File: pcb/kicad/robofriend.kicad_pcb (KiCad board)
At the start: 2 copper layers, 122 parts, among them J1 UART, J10 12V-Buck, J11 12V-Buck-Boost, J12 5VIN, J13 5VOUT, J14 5VOUT, J15 US2, J16 US3, J17 USB_A_4_PIN, J18 12V-Reg, J19 MON/AMP, J2 PWR, J20 US4, J21 MRi, J22 SPI, J23 MLe, J24 3V3OUT, J25 3V3OUT, J26 M1, J27 M2, J28 IR1, J29 ADC1, J3 PWR, J30 IR2, J31 ADC2, J32 IR3, J33 GS2, J4 GS2, J5 I2C, J6 I2C, J7 I2C, J8 I2C, J9 US1, K1 SCHRACK-RTx3, Q1 NMOS, Q2 NPN, Q3 PMOS, U1 74LVC1T45, U10 TL331, U2 Teensy++2.0, U3 TL331, U4 74LVC1T45, U5 PCA9517, U6 MCP6001, U7 LM3940-3.3, U8 LM4040, U9 INA193

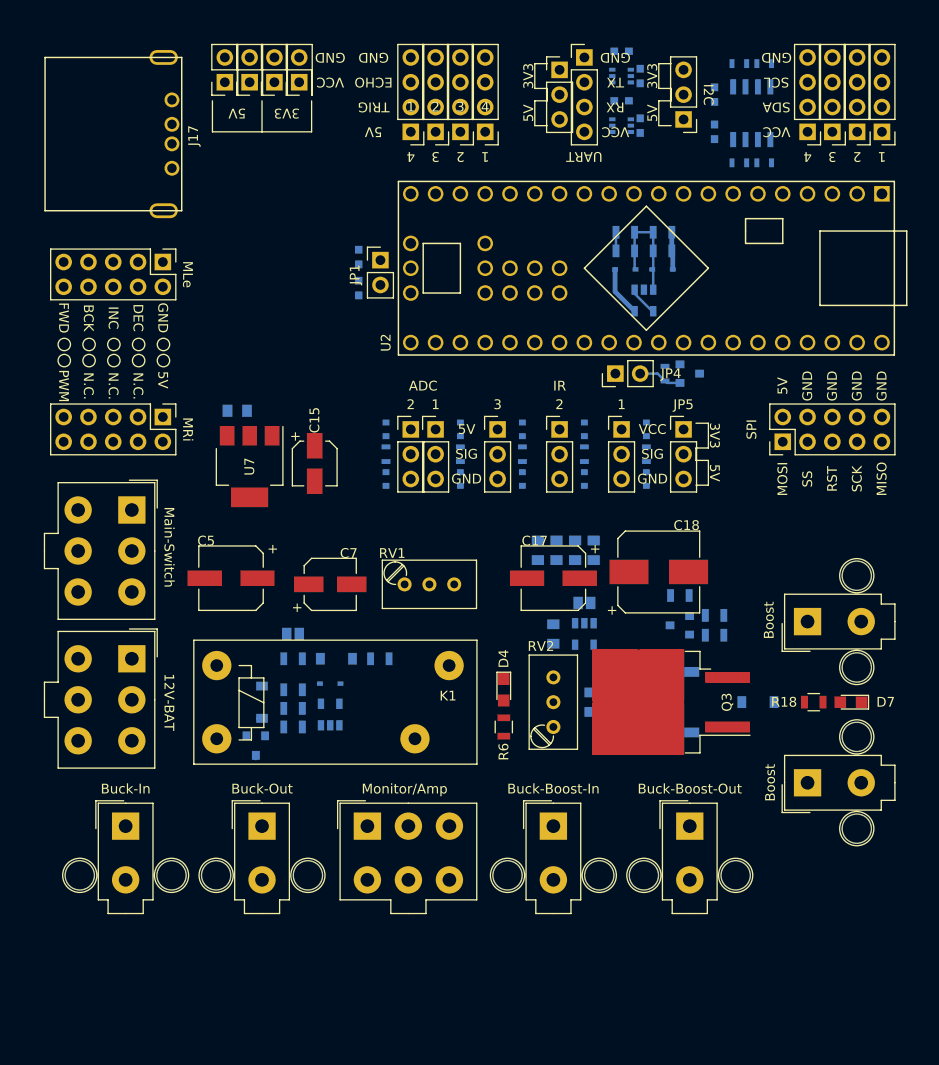
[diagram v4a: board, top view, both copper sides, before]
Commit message: defined board edge cuts
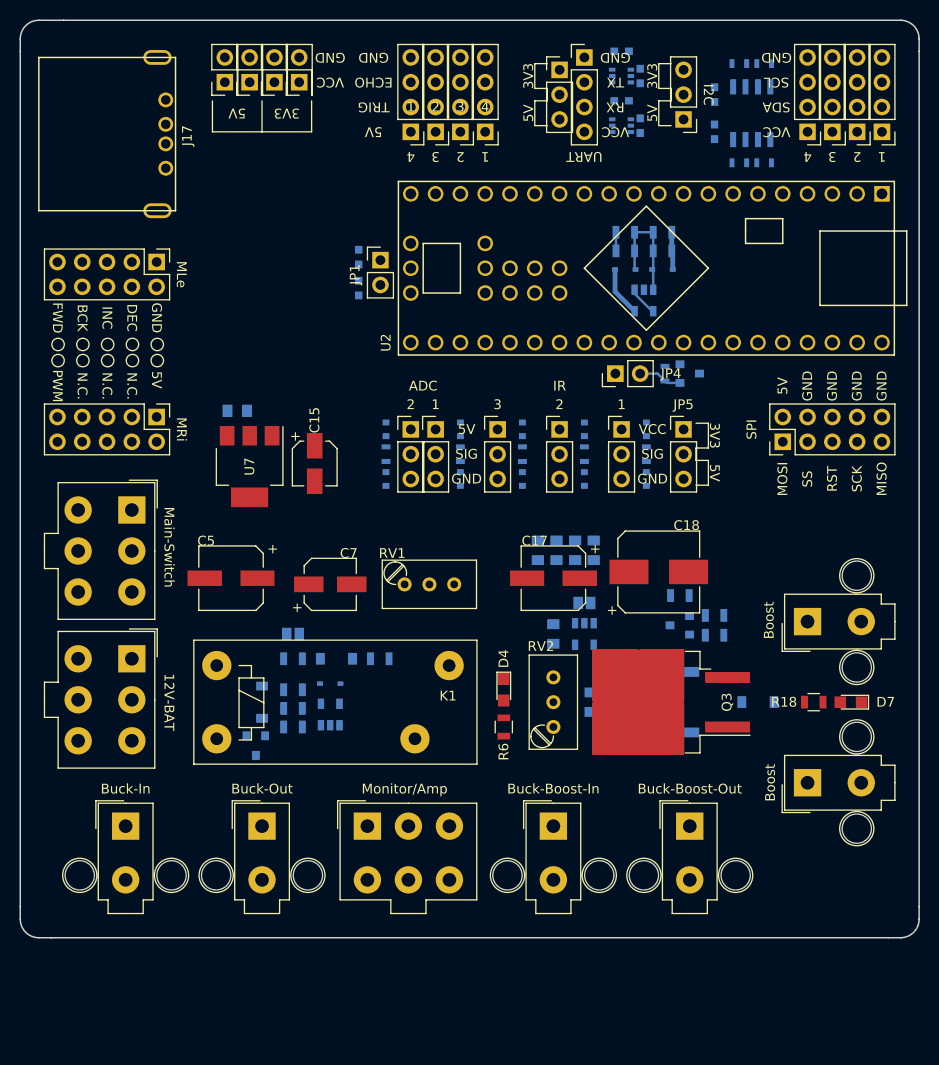
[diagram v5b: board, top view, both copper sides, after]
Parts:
- moved J17 0.64 mm to (82.5, 71.1)
- moved J21 0.64 mm to (94.6, 108.0)
- moved J23 0.64 mm to (94.6, 92.1)
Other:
- board outline added: 92.1 x 94 mm
- net class 10A: clearance 0.2 -> 0.254
- net class 3A: clearance 0.2 -> 0.254
- net class 5A: clearance 0.2 -> 0.254
- net class Default: clearance 0.2 -> 0.254; trace_width 0.25 -> 0.254
- rule trace_clearance: 0.2 -> 0.254
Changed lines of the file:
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@@
     (links 300)
     (no_connects 285)
-    (area 80.93 67.38 172.315 159.385001)
+    (area 80.295 67.234999 172.795001 161.365001)
     (thickness 1.6)
-    (drawings 119)
+    (drawings 134)
     (tracks 28)
     (zones 0)
@@
   )
   (setup
-    (last_trace_width 0.25)
-    (trace_clearance 0.2)
+    (last_trace_width 0.254)
+    (trace_clearance 0.254)
     (zone_clearance 0.508)
     (zone_45_only no)
     (trace_min 0.2)
-    (segment_width 0.1)
+    (segment_width 0.35)
     (edge_width 0.15)
     (via_size 0.6)
@@
   (net 77 "Net-(JP4-Pad2)")
   (net_class Default "This is the default net class."
-    (clearance 0.2)
-    (trace_width 0.25)
+    (clearance 0.254)
+    (trace_width 0.254)
     (via_dia 0.6)
     (via_drill 0.4)
@@
   )
   (net_class 10A ""
-    (clearance 0.2)
+    (clearance 0.254)
     (trace_width 2)
     (via_dia 0.6)
@@
   )
   (net_class 3A ""
-    (clearance 0.2)
+    (clearance 0.254)
     (trace_width 0.48)
     (via_dia 0.6)
@@
   )
   (net_class 5A ""
-    (clearance 0.2)
+    (clearance 0.254)
     (trace_width 0.96)
     (via_dia 0.6)
@@
     (tags "capacitor 0805")
     (attr smd)
-    (fp_text reference C11 (at -0.3175 -1.5875) (layer B.SilkS)
+    (fp_text reference C11 (at 0 -1.905) (layer B.SilkS)
       (effects (font (size 1 1) (thickness 0.15)) (justify mirror))
     )
@@
   )
   (module Pin_Headers:Pin_Header_Straight_2x05_Pitch2.54mm (layer F.Cu)
-    (at 95.25 107.95 270)
+    (at 94.615 107.95 270)
     (descr "Through hole straight pin header, 2x05, 2.54mm pitch, double rows")
     (tags "Through hole pin header THT 2x05 2.54mm double row")
@@
   )
   (module Pin_Headers:Pin_Header_Straight_2x05_Pitch2.54mm (layer F.Cu)
-    (at 95.25 92.075 270)
+    (at 94.615 92.075 270)
     (descr "Through hole straight pin header, 2x05, 2.54mm pitch, double rows")
     (tags "Through hole pin header THT 2x05 2.54mm double row")
@@
   )
   (module USB_A_4_PIN:MOLEX_48258_0001 (layer F.Cu)
-    (at 83.185 71.12 270)
+    (at 82.55 71.12 270)
     (descr "USB A connector")
     (tags "USB USB_A")
@@
     )
   )
+  (gr_arc (start 82.55 159.385) (end 82.55 161.29) (angle 90) (layer Edge.Cuts) (width 0.15))
+  (gr_arc (start 170.815 159.385) (end 172.72 159.385) (angle 90) (layer Edge.Cuts) (width 0.15))
+  (gr_arc (start 170.815 69.215) (end 170.815 67.31) (angle 90) (layer Edge.Cuts) (width 0.15))
+  (gr_arc (start 82.55 69.215) (end 80.645 69.215) (angle 90) (layer Edge.Cuts) (width 0.15))
+  (gr_line (start 85.09 67.31) (end 82.55 67.31) (angle 90) (layer Edge.Cuts) (width 0.15))
+  (gr_line (start 80.645 70.485) (end 80.645 69.215) (angle 90) (layer Edge.Cuts) (width 0.15))
+  (gr_line (start 83.82 161.29) (end 82.55 161.29) (angle 90) (layer Edge.Cuts) (width 0.15))
+  (gr_line (start 80.645 158.115) (end 80.645 159.385) (angle 90) (layer Edge.Cuts) (width 0.15))
+  (gr_line (start 170.815 161.29) (end 169.545 161.29) (angle 90) (layer Edge.Cuts) (width 0.15))
+  (gr_line (start 172.72 159.385) (end 172.72 158.115) (angle 90) (layer Edge.Cuts) (width 0.15))
+  (gr_line (start 172.72 70.485) (end 172.72 69.215) (angle 90) (layer Edge.Cuts) (width 0.15))
+  (gr_line (start 80.645 158.115) (end 80.645 70.485) (angle 90) (layer Edge.Cuts) (width 0.15))
+  (gr_line (start 169.545 161.29) (end 83.82 161.29) (angle 90) (layer Edge.Cuts) (width 0.15))
+  (gr_line (start 172.72 70.485) (end 172.72 158.115) (angle 90) (layer Edge.Cuts) (width 0.15))
+  (gr_line (start 85.09 67.31) (end 170.815 67.31) (angle 90) (layer Edge.Cuts) (width 0.15))
   (gr_line (start 133.35 71.755) (end 133.35 74.295) (angle 90) (layer F.SilkS) (width 0.1))
   (gr_line (start 134.62 74.295) (end 134.62 75.565) (angle 90) (layer F.SilkS) (width 0.1))
@@
     (effects (font (size 1 1) (thickness 0.15)))
   )
-  (gr_circle (center 85.1535 100.5205) (end 85.1535 101.1555) (layer F.SilkS) (width 0.1))
-  (gr_circle (center 85.1535 102.1715) (end 85.1535 102.8065) (layer F.SilkS) (width 0.1))
-  (gr_circle (center 90.2335 100.5205) (end 90.2335 101.1555) (layer F.SilkS) (width 0.1))
-  (gr_circle (center 90.2335 102.1715) (end 90.2335 102.8065) (layer F.SilkS) (width 0.1))
-  (gr_circle (center 87.6935 102.1715) (end 87.6935 102.8065) (layer F.SilkS) (width 0.1))
-  (gr_circle (center 87.6935 100.5205) (end 87.6935 101.1555) (layer F.SilkS) (width 0.1))
-  (gr_circle (center 92.7735 100.5205) (end 92.7735 101.1555) (layer F.SilkS) (width 0.1))
-  (gr_circle (center 92.7735 102.1715) (end 92.7735 102.8065) (layer F.SilkS) (width 0.1))
-  (gr_circle (center 95.3135 102.1715) (end 95.3135 102.8065) (layer F.SilkS) (width 0.1))
-  (gr_circle (center 95.3135 100.5205) (end 95.3135 101.1555) (layer F.SilkS) (width 0.1))
-  (gr_text 5V (at 95.25 104.14 270) (layer F.SilkS)
+  (gr_circle (center 84.5185 100.5205) (end 84.5185 101.1555) (layer F.SilkS) (width 0.1))
+  (gr_circle (center 84.5185 102.1715) (end 84.5185 102.8065) (layer F.SilkS) (width 0.1))
+  (gr_circle (center 89.5985 100.5205) (end 89.5985 101.1555) (layer F.SilkS) (width 0.1))
+  (gr_circle (center 89.5985 102.1715) (end 89.5985 102.8065) (layer F.SilkS) (width 0.1))
+  (gr_circle (center 87.0585 102.1715) (end 87.0585 102.8065) (layer F.SilkS) (width 0.1))
+  (gr_circle (center 87.0585 100.5205) (end 87.0585 101.1555) (layer F.SilkS) (width 0.1))
+  (gr_circle (center 92.1385 100.5205) (end 92.1385 101.1555) (layer F.SilkS) (width 0.1))
+  (gr_circle (center 92.1385 102.1715) (end 92.1385 102.8065) (layer F.SilkS) (width 0.1))
+  (gr_circle (center 94.6785 102.1715) (end 94.6785 102.8065) (layer F.SilkS) (width 0.1))
+  (gr_circle (center 94.6785 100.5205) (end 94.6785 101.1555) (layer F.SilkS) (width 0.1))
+  (gr_text 5V (at 94.615 104.14 270) (layer F.SilkS)
     (effects (font (size 1 1) (thickness 0.15)))
   )
-  (gr_text PWM (at 85.09 104.775 270) (layer F.SilkS)
+  (gr_text PWM (at 84.455 104.775 270) (layer F.SilkS)
     (effects (font (size 1 1) (thickness 0.15)))
   )
@@
     (effects (font (size 1 1) (thickness 0.15)))
   )
-  (gr_text N.C. (at 92.71 104.775 270) (layer F.SilkS)
+  (gr_text N.C. (at 92.075 104.775 270) (layer F.SilkS)
     (effects (font (size 1 1) (thickness 0.15)))
   )
-  (gr_text N.C. (at 90.17 104.775 270) (layer F.SilkS)
+  (gr_text N.C. (at 89.535 104.775 270) (layer F.SilkS)
     (effects (font (size 1 1) (thickness 0.15)))
   )
-  (gr_text N.C. (at 87.63 104.775 270) (layer F.SilkS)
+  (gr_text N.C. (at 86.995 104.775 270) (layer F.SilkS)
     (effects (font (size 1 1) (thickness 0.15)))
   )
-  (gr_text FWD (at 85.09 97.79 270) (layer F.SilkS)
+  (gr_text FWD (at 84.455 97.79 270) (layer F.SilkS)
     (effects (font (size 1 1) (thickness 0.15)))
   )
-  (gr_text BCK (at 87.63 97.79 270) (layer F.SilkS)
+  (gr_text BCK (at 86.995 97.79 270) (layer F.SilkS)
     (effects (font (size 1 1) (thickness 0.15)))
   )
-  (gr_text INC (at 90.17 97.79 270) (layer F.SilkS)
+  (gr_text INC (at 89.535 97.79 270) (layer F.SilkS)
     (effects (font (size 1 1) (thickness 0.15)))
   )
-  (gr_text DEC (at 92.71 97.79 270) (layer F.SilkS)
+  (gr_text DEC (at 92.075 97.79 270) (layer F.SilkS)
     (effects (font (size 1 1) (thickness 0.15)))
   )
@@
     (effects (font (size 1 1) (thickness 0.15)))
   )
-  (gr_text GND (at 95.25 97.79 270) (layer F.SilkS)
+  (gr_text GND (at 94.615 97.79 270) (layer F.SilkS)
     (effects (font (size 1 1) (thickness 0.15)))
   )
@@
     (effects (font (size 1 1) (thickness 0.15)))
   )
-  (gr_text "RoboFriend - Power PCB \nDesigned by Martin Zahedi \nUniversity of Applied Sciences - Technikum Wien" (at 108.585 99.06 90) (layer B.SilkS)
+  (gr_text "RoboFriend - Power PCB \nDesigned by Martin Zahedi \nUniversity of Applied Sciences - Technikum Wien" (at 107.95 99.06 90) (layer B.SilkS)
     (effects (font (size 1 1) (thickness 0.15)) (justify mirror))
   )
@@
     (effects (font (size 1 1) (thickness 0.15)))
   )
-  (gr_text MLe (at 97.79 93.345 270) (layer F.SilkS)
+  (gr_text MLe (at 97.155 93.345 270) (layer F.SilkS)
     (effects (font (size 1 1) (thickness 0.15)))
   )
-  (gr_text MRi (at 97.79 109.22 270) (layer F.SilkS)
+  (gr_text MRi (at 97.155 109.22 270) (layer F.SilkS)
     (effects (font (size 1 1) (thickness 0.15)))
   )

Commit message: starting bom
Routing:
- net Net-(D5-Pad2): track 11.7 -> 0.00 mm
- net +5V: track 5.25 -> 0.00 mm
- net Net-(JP4-Pad2): track 4.47 -> 0.00 mm
- net GND: track 4.44 -> 0.00 mm
- net F0: track 3.05 -> 0.00 mm
- net +12V: track 1.91 -> 0.00 mm
- net Net-(D3-Pad2): track 0.81 -> 0.00 mm
- added copper zone on B.Cu, net GND
- added copper zone on F.Cu, net GND
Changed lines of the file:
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@@
   (general
     (links 300)
-    (no_connects 285)
-    (area 80.295 67.234999 172.795001 161.365001)
+    (no_connects 214)
+    (area 80.569999 67.234999 172.795001 161.365001)
     (thickness 1.6)
     (drawings 134)
-    (tracks 28)
+    (tracks 0)
     (zones 0)
     (modules 122)
@@
     (effects (font (size 1.5 1.5) (thickness 0.3)))
   )
-  (segment (start 147.481 92.837) (end 147.481 91.032) (width 0.48) (layer B.Cu) (net 1))
-  (segment (start 147.481 91.032) (end 147.381 90.932) (width 0.48) (layer B.Cu) (net 1))
-  (segment (start 147.381 90.932) (end 147.381 89.027) (width 0.48) (layer B.Cu) (net 1))
-  (segment (start 107.635 139.7) (end 107.635 140.02) (width 0.48) (layer B.Cu) (net 1))
-  (segment (start 104.775 142.605) (end 104.775 142.875) (width 0.48) (layer B.Cu) (net 1))
-  (segment (start 141.571 92.837) (end 141.571 95.107) (width 0.48) (layer B.Cu) (net 2))
-  (segment (start 141.571 95.107) (end 143.576 97.112) (width 0.48) (layer B.Cu) (net 2))
-  (segment (start 135.355 131.275) (end 135.255 131.175) (width 0.48) (layer B.Cu) (net 2))
-  (segment (start 145.476 97.112) (end 145.372 97.112) (width 0.25) (layer B.Cu) (net 7))
-  (segment (start 145.372 97.112) (end 143.576 95.316) (width 0.25) (layer B.Cu) (net 7))
-  (segment (start 143.576 95.316) (end 143.576 94.912) (width 0.25) (layer B.Cu) (net 7))
-  (segment (start 141.671 89.027) (end 141.671 90.932) (width 0.25) (layer B.Cu) (net 47))
-  (segment (start 101.08 140.605) (end 100.775 140.91) (width 0.48) (layer B.Cu) (net 48))
-  (segment (start 105.41 138.81) (end 105.03 138.81) (width 0.48) (layer B.Cu) (net 48))
-  (segment (start 139.38 127.31) (end 139.07 127) (width 0.25) (layer B.Cu) (net 53))
-  (segment (start 118.425 132.4) (end 118.425 132.715) (width 0.48) (layer B.Cu) (net 55))
-  (segment (start 145.476 94.912) (end 145.476 92.932) (width 0.25) (layer B.Cu) (net 58))
-  (segment (start 145.476 92.932) (end 145.381 92.837) (width 0.25) (layer B.Cu) (net 58))
-  (segment (start 145.481 89.027) (end 145.481 92.737) (width 0.25) (layer B.Cu) (net 58))
-  (segment (start 145.481 92.737) (end 145.381 92.837) (width 0.25) (layer B.Cu) (net 58))
-  (segment (start 143.571 89.027) (end 145.481 89.027) (width 0.25) (layer B.Cu) (net 58))
-  (segment (start 143.571 89.027) (end 143.571 92.737) (width 0.25) (layer B.Cu) (net 58))
-  (segment (start 143.571 92.737) (end 143.671 92.837) (width 0.25) (layer B.Cu) (net 58))
-  (segment (start 143.29 136.16) (end 143.19 136.06) (width 0.48) (layer B.Cu) (net 70))
-  (segment (start 109.22 130.18) (end 109.225 130.175) (width 0.48) (layer B.Cu) (net 74))
-  (segment (start 144.145 103.505) (end 145.935 103.505) (width 0.25) (layer B.Cu) (net 77))
-  (segment (start 145.935 103.505) (end 146.885 104.455) (width 0.25) (layer B.Cu) (net 77))
-  (segment (start 146.885 104.455) (end 148.225 104.455) (width 0.25) (layer B.Cu) (net 77))
+  (zone (net 1) (net_name GND) (layer B.Cu) (hatch edge 0.508)
+    (connect_pads (clearance 0.508))
+    (min_thickness 0.254)
+    (fill yes (arc_segments 16) (thermal_gap 0.508) (thermal_bridge_width 0.508))
+    (polygon
+      (pts
+        (xy 81.28 67.945) (xy 172.085 67.945) (xy 172.085 160.655) (xy 81.28 160.655)
+      )
+    )
+  )
+  (zone (net 1) (net_name GND) (layer F.Cu) (hatch edge 0.508)
+    (connect_pads (clearance 0.508))
+    (min_thickness 0.254)
+    (fill yes (arc_segments 16) (thermal_gap 0.508) (thermal_bridge_width 0.508))
+    (polygon
+      (pts
+        (xy 81.28 67.945) (xy 172.085 67.945) (xy 172.085 160.655) (xy 81.28 160.655)
+      )
+    )
+  )
 )

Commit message: correction on 74LVC1T45 circuit, DIR ref to VCCA, updated netlist in layout
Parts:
- J2: value PWR -> VBAT
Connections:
- U1 pad 1: Net-(C3-Pad1) -> +5V
- U1 pad 3: Rx -> D3
- U1 pad 4: D2 -> Tx
- U1 pad 6: +5V -> Net-(C3-Pad1)
- U4 pad 1: Net-(C3-Pad1) -> +5V
- U4 pad 3: Tx -> D2
- U4 pad 4: D3 -> Rx
- U4 pad 6: +5V -> Net-(C3-Pad1)
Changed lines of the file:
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@@
   (general
     (links 300)
-    (no_connects 214)
+    (no_connects 296)
     (area 80.569999 67.234999 172.795001 161.365001)
     (thickness 1.6)
@@
       (effects (font (size 1 1) (thickness 0.15)))
     )
-    (fp_text value PWR (at 4.2 -4 270) (layer F.Fab)
+    (fp_text value VBAT (at 4.2 -4 270) (layer F.Fab)
       (effects (font (size 1 1) (thickness 0.15)))
     )
@@
     (fp_line (start -0.175 1.1) (end -0.675 0.6) (layer B.Fab) (width 0.1))
     (pad 1 smd rect (at -0.95 0.65) (size 0.65 0.4) (layers B.Cu B.Paste B.Mask)
-      (net 67 "Net-(C3-Pad1)"))
+      (net 2 +5V))
     (pad 3 smd rect (at -0.95 -0.65) (size 0.65 0.4) (layers B.Cu B.Paste B.Mask)
-      (net 72 Rx))
+      (net 15 D3))
     (pad 5 smd rect (at 0.95 0) (size 0.65 0.4) (layers B.Cu B.Paste B.Mask)
       (net 2 +5V))
@@
       (net 1 GND))
     (pad 4 smd rect (at 0.95 -0.65) (size 0.65 0.4) (layers B.Cu B.Paste B.Mask)
-      (net 14 D2))
+      (net 73 Tx))
     (pad 6 smd rect (at 0.95 0.65) (size 0.65 0.4) (layers B.Cu B.Paste B.Mask)
-      (net 2 +5V))
+      (net 67 "Net-(C3-Pad1)"))
     (model ${KISYS3DMOD}/TO_SOT_Packages_SMD.3dshapes/SOT-363_SC-70-6.wrl
       (at (xyz 0 0 0))
@@
     (fp_line (start -0.175 1.1) (end -0.675 0.6) (layer B.Fab) (width 0.1))
     (pad 1 smd rect (at -0.95 0.65) (size 0.65 0.4) (layers B.Cu B.Paste B.Mask)
-      (net 67 "Net-(C3-Pad1)"))
+      (net 2 +5V))
     (pad 3 smd rect (at -0.95 -0.65) (size 0.65 0.4) (layers B.Cu B.Paste B.Mask)
-      (net 73 Tx))
+      (net 14 D2))
     (pad 5 smd rect (at 0.95 0) (size 0.65 0.4) (layers B.Cu B.Paste B.Mask)
       (net 1 GND))
@@
       (net 1 GND))
     (pad 4 smd rect (at 0.95 -0.65) (size 0.65 0.4) (layers B.Cu B.Paste B.Mask)
-      (net 15 D3))
+      (net 72 Rx))
     (pad 6 smd rect (at 0.95 0.65) (size 0.65 0.4) (layers B.Cu B.Paste B.Mask)
-      (net 2 +5V))
+      (net 67 "Net-(C3-Pad1)"))
     (model ${KISYS3DMOD}/TO_SOT_Packages_SMD.3dshapes/SOT-363_SC-70-6.wrl
       (at (xyz 0 0 0))
@@
     (connect_pads (clearance 0.508))
     (min_thickness 0.254)
-    (fill yes (arc_segments 16) (thermal_gap 0.508) (thermal_bridge_width 0.508))
+    (fill (arc_segments 16) (thermal_gap 0.508) (thermal_bridge_width 0.508))
     (polygon
       (pts
@@
     (connect_pads (clearance 0.508))
     (min_thickness 0.254)
-    (fill yes (arc_segments 16) (thermal_gap 0.508) (thermal_bridge_width 0.508))
+    (fill (arc_segments 16) (thermal_gap 0.508) (thermal_bridge_width 0.508))
     (polygon
       (pts
